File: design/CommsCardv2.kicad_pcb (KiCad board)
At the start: 4 copper layers, 204 parts, among them J1001 USB_B, J201 Conn_01x02, J301 DB9_Male_MountingHoles, J302 DB9_Male_MountingHoles, J303 DB9_Male_MountingHoles, J304 Conn_01x02, J305 Conn_Coaxial, J501 Conn_01x03, J701 Conn_01x03, J901 USB_B, Q301 Q_NMOS_DGS, Q302 Q_NMOS_DGS, U1001 ADUM3160, U201 LT3509EMSE, U301 MAX3387EEUG, U302 MAX3485, U303 TPS28225DRBT, U401 STWD100xxWY, U402 STWD100xxWY, U403 74LVC2G00, U405 74AHC157, U406 74LV14, U501 93C46B, U502 FT4232H, U503 74LV595, U601 SN74LV86, U602 74LVC3G14, U603 74LVC1G80, U604 74LVC2G86, U605 74LV595, U606 74LV595, U607 74LVC2G86, U701 93C46B, U702 FT4232H, U703 74LV595, U801 SN74LV86, U802 74LVC3G14, U803 74LVC1G80, U804 74LV595, U805 74LVC2G86, U806 74LV595, U807 74LVC2G86, U808 74LVC3G14, U809 74LVC3G14, U810 74LVC3G14, U901 ADUM3160, Y501 ABM8G, Y701 ABM8G

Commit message: Placing caps
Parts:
- removed C502, C505, C702, C705: 27pF, Capacitor_SMD:C_0603_1608Metric
- removed Y501, Y701: ABM8G, Crystal:Crystal_SMD_Abracon_ABM8G-4Pin_3.2x2.5mm
- added C516: 10nF, Capacitor_SMD:C_0603_1608Metric, F.Cu at (158.8, 74.9)
- added C716: 10nF, Capacitor_SMD:C_0603_1608Metric, F.Cu at (187.5, 74.0)
- added R513: 10k, Resistor_SMD:R_0603_1608Metric, F.Cu at (167.0, 71.1)
- added R713: 10k, Resistor_SMD:R_0603_1608Metric, F.Cu at (187.5, 68.6)
- added X501: ASEMB-12MHz, Oscillator:Oscillator_SMD_Abracon_ASE-4Pin_3.2x2.5mm, F.Cu at (158.8, 72.5)
- added X701: ASEMB-12MHz, Oscillator:Oscillator_SMD_Abracon_ASE-4Pin_3.2x2.5mm, F.Cu at (179.5, 69.4)
- L501, L502, L701, L702: footprint Resistor_SMD:R_0603_1608Metric -> Resistor_SMD:R_1210_3225Metric
- moved L502 170.6 mm to (164.5, 66.0), turned to 90 degrees
- moved C508 166.3 mm to (148.0, 71.1), turned to 270 degrees
- moved R509 156.2 mm to (163.8, 79.5)
- moved C513 155.8 mm to (154.9, 71.1), turned to 90 degrees
- moved L501 154.4 mm to (141.0, 66.7), turned to 180 degrees
- moved R510 152.2 mm to (163.8, 76.9)
- moved R507 150.3 mm to (141.6, 79.5), turned to 180 degrees
- moved R508 148.2 mm to (148.6, 85.1), turned to 270 degrees
- moved C507 146.5 mm to (158.8, 82.6)
- moved C512 145.6 mm to (142.2, 74.9), turned to 180 degrees
- moved C514 145.0 mm to (146.7, 85.1), turned to 270 degrees
- moved C506 144.0 mm to (153.0, 71.1), turned to 90 degrees
- moved R511 141.4 mm to (163.8, 75.0)
- moved C501 139.5 mm to (161.9, 66.7), turned to 90 degrees
- moved C510 134.5 mm to (158.8, 77.5)
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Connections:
- net Net-(R501-Pad2) renamed /FlightComputer1/REF
- net Net-(R701-Pad2) renamed /FlightComputer2/REF
- C503 pad 1: Net-(C501-Pad1) -> Net-(C503-Pad1)
- C508 pad 1: Net-(C501-Pad1) -> Net-(C503-Pad1)
- C703 pad 1: Net-(C701-Pad1) -> Net-(C703-Pad1)
- C708 pad 1: Net-(C701-Pad1) -> Net-(C703-Pad1)
- L501 pad 1: Net-(C501-Pad1) -> Net-(C503-Pad1)
- L502 pad 1: GND -> Net-(C501-Pad1)
- L701 pad 1: Net-(C701-Pad1) -> Net-(C703-Pad1)
- L702 pad 1: GND -> Net-(C701-Pad1)
- U502 pad 3: Net-(C502-Pad1) -> /FlightComputer1/OSCI
- U502 pad 5: GND -> Net-(C501-Pad1)
- U502 pad 9: Net-(C501-Pad1) -> Net-(C503-Pad1)
- U702 pad 3: Net-(C702-Pad1) -> /FlightComputer2/OSCI
- U702 pad 5: GND -> Net-(C701-Pad1)
- U702 pad 9: Net-(C701-Pad1) -> Net-(C703-Pad1)
- U810 pad 3: Net-(U810-Pad3) -> (no net)
- U810 pad 4: (no net) -> GND
- U810 pad 5: Net-(U810-Pad5) -> (no net)
- U810 pad 8: (no net) -> +3V3

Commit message: Annotating
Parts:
- removed the C509 at (103.4, 219.3)
- removed C515, C608, C609, C715, C808, C809: 0u1F, Capacitor_SMD:C_0603_1608Metric
- removed the C601 at (89.5, 253.4)
- removed the C709 at (213.0, 159.5)
- removed the C801 at (155.2, 250.9)
- removed the U607 at (100.8, 248.3)
- removed the U802 at (144.4, 246.7)
- removed the U805 at (169.8, 236.6)
- removed U807: 74LVC2G86, Package_SO:MSOP-8_3x3mm_P0.65mm
- removed U808, U809, U810: 74LVC3G14, Package_SO:VSSOP-8_2.3x2mm_P0.5mm
- added C602: 0u1F, Capacitor_SMD:C_0603_1608Metric, F.Cu at (54.0, 156.9)
- added C802: 0u1F, Capacitor_SMD:C_0603_1608Metric, F.Cu at (69.8, 156.9)
- added U801: 74LVC3G14, Package_SO:VSSOP-8_2.3x2mm_P0.5mm, F.Cu at (161.9, 246.4)
- added U803: 501BMILF, Package_SO:SOIC-8_3.9x4.9mm_P1.27mm, F.Cu at (63.6, 158.8)
- U603: value 74LVC1G80 -> 501BMILF; footprint Package_TO_SOT_SMD:SOT-353_SC-70-5 -> Package_SO:SOIC-8_3.9x4.9mm_P1.27mm
- U604: value 74LVC2G86 -> 74LVC1G80; footprint Package_SO:MSOP-8_3x3mm_P0.65mm -> Package_TO_SOT_SMD:SOT-353_SC-70-5
- moved C606 188.7 mm to (132.1, 68.6)
- moved U601 186.2 mm to (128.3, 68.6)
- moved D502 182.3 mm to (172.7, 41.3)
- moved U603 175.3 mm to (125.1, 75.6)
- moved D503 174.3 mm to (165.1, 41.3)
- moved U602 169.8 mm to (133.3, 75.6), turned to 180 degrees
- moved U604 159.2 mm to (128.9, 81.3)
- moved C603 155.7 mm to (116.2, 82.5)
- moved U605 150.4 mm to (122.6, 91.4)
- moved U607 146.0 mm to (123.2, 99.7)
- moved J501 135.8 mm to (134.0, 82.5)
- moved X701 92.7 mm to (88.7, 87.9)
- moved C702 92.7 mm to (96.7, 92.4)
- moved R701 92.7 mm to (96.7, 87.1)
- moved D501 5.86 mm to (180.3, 41.3)
- renumbered C405 to C401, C401 to C402, C402 to C403, C403 to C404, C404 to C405, C503 to C501, C516 to C502, C501 to C503, C508 to C504, C506 to C505, C504 to C506, C510 to C508, C511 to C509, C512 to C510, C513 to C511, C514 to C512, C605 to C601, C606 to C605, C602 to C606, C703 to C701, C716 to C702, C701 to C703, C708 to C704, C706 to C705, C704 to C706, C710 to C708, C711 to C709, C712 to C710, C713 to C711, C714 to C712, C803 to C801, C805 to C803, C807 to C805, C802 to C807, R404 to R403, R405 to R404, R406 to R405, R407 to R406, R403 to R407, R513 to R501, R501 to R502, R502 to R503, R503 to R504, R504 to R505, R505 to R506, R506 to R507, R507 to R508, R508 to R509, R509 to R510, R510 to R511, R511 to R512, R512 to R513, R713 to R701, R701 to R702, R702 to R703, R703 to R704, R704 to R705, R705 to R706, R706 to R707, R707 to R708, R708 to R709, R709 to R710, R710 to R711, R711 to R712, R712 to R713, U406 to U401, U403 to U402, U401 to U403, U402 to U404, U602 to U601, U601 to U602, U606 to U607, U801 to U802, U803 to U804, U804 to U805
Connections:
- U601 pad 3: Net-(C601-Pad1) -> (no net)
- U601 pad 5: Net-(C601-Pad2) -> (no net)
- U602 pad 10: /FlightComputer1/LOSComms/DELAY_CLK -> Net-(U602-Pad10)
- U602 pad 3: Net-(U601-Pad3) -> Net-(U602-Pad3)
- U602 pad 4: /FlightComputer1/LOSComms/DELAY_CLK -> /FlightComputer1/LOSComms/DATA
- U602 pad 5: GND -> Net-(U602-Pad5)
- U602 pad 6: Net-(C601-Pad1) -> /FlightComputer1/LOSComms/RNRZ-L
- U602 pad 8: Net-(U601-Pad8) -> Net-(U602-Pad5)
- U602 pad 9: Net-(C601-Pad2) -> Net-(U602-Pad9)
- U603 pad 1: Net-(U601-Pad3) -> /FlightComputer1/LOSComms/DELAY_CLK
- U603 pad 2: Net-(U601-Pad8) -> +3V3
- U603 pad 4: /FlightComputer1/LOSComms/BIPHASE -> Net-(U603-Pad4)
- U603 pad 5: +3V3 -> Net-(U603-Pad5)
- U604 pad 1: /FlightComputer1/LOSComms/DATA -> Net-(U602-Pad3)
- U604 pad 2: Net-(U604-Pad2) -> Net-(U603-Pad5)
- U604 pad 3: Net-(U604-Pad2) -> GND
- U604 pad 4: GND -> /FlightComputer1/LOSComms/BIPHASE
- U604 pad 5: Net-(U604-Pad5) -> +3V3
- U607 pad 4: Net-(U604-Pad5) -> Net-(U602-Pad9)
- U607 pad 5: Net-(U604-Pad6) -> Net-(U602-Pad10)
- U802 pad 10: /FlightComputer2/LOSComms/DELAY_CLK -> Net-(U802-Pad10)
- U802 pad 4: /FlightComputer2/LOSComms/DELAY_CLK -> /FlightComputer2/LOSComms/DATA
- U802 pad 5: GND -> Net-(U802-Pad5)
- U802 pad 6: Net-(C801-Pad1) -> /FlightComputer2/LOSComms/RNRZ-L
- U802 pad 8: Net-(U801-Pad8) -> Net-(U802-Pad5)
- U802 pad 9: Net-(C801-Pad2) -> Net-(U802-Pad9)
- U804 pad 2: Net-(U801-Pad8) -> Net-(U803-Pad5)
- U806 pad 4: Net-(U607-Pad5) -> Net-(U802-Pad9)
- U806 pad 5: Net-(U607-Pad6) (its old number) -> Net-(U802-Pad10)

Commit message: Further Layout work
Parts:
- moved C202 185.2 mm to (122.6, 46.4)
- moved C310 184.0 mm to (330.4, 103.5)
- moved C209 178.6 mm to (111.1, 47.0), turned to 90 degrees
- moved C207 176.9 mm to (120.0, 57.1)
- moved R203 173.3 mm to (118.7, 66.7), turned to 90 degrees
- moved L202 173.1 mm to (118.1, 48.3)
- moved C201 172.1 mm to (122.6, 48.9)
- moved C206 171.8 mm to (125.1, 57.1), turned to 180 degrees
- moved R205 171.7 mm to (117.9, 64.1), turned to 180 degrees
- moved R204 169.9 mm to (127.2, 64.1)
- moved R202 166.4 mm to (126.4, 66.7), turned to 90 degrees
- moved C205 166.0 mm to (120.7, 66.7), turned to 270 degrees
- moved R201 165.2 mm to (122.6, 66.7), turned to 270 degrees
- moved C204 164.4 mm to (124.5, 66.7), turned to 270 degrees
- moved D202 164.2 mm to (116.8, 52.7), turned to 180 degrees
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- renumbered C603 to C601, C601 to C603, C607 to C605, C605 to C606, C606 to C607, U607 to U606
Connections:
- net Net-(C206-Pad1) renamed /Power/BOOST1
- net Net-(C206-Pad2) renamed /Power/SW1
- net Net-(C207-Pad1) renamed /Power/BOOST2
- net Net-(C207-Pad2) renamed /Power/SW2
- net Net-(D201-Pad2) renamed /Power/DA1
- net Net-(D202-Pad2) renamed /Power/DA2
- net Net-(R202-Pad2) renamed /Power/FB1
- net Net-(R203-Pad2) renamed /Power/FB2
- net Net-(U402-Pad6) renamed /Watchdog/FC2_WDO
- U402 pad 1: Net-(U402-Pad1) -> /FlightComputer1/IN_CHARGE
- U402 pad 2: Net-(U402-Pad2) -> /Watchdog/FC1_WDO
- U402 pad 3: Net-(U402-Pad2) -> Net-(R407-Pad1)
- U402 pad 5: /FlightComputer1/IN_CHARGE -> Net-(U402-Pad5)
- U402 pad 7: Net-(R407-Pad1) -> Net-(U402-Pad5)
- U403 pad 1: Net-(U402-Pad1) -> /Watchdog/FC1_WDO
- U601 pad 3: (no net) -> Net-(C807-Pad1)
- U601 pad 5: (no net) -> /FlightComputer2/LOSComms/DELAY_CLK
- U801 pad 3: Net-(C807-Pad1) -> (no net)
- U801 pad 5: /FlightComputer2/LOSComms/DELAY_CLK -> (no net)

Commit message: Further routing
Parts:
- moved R701 125.8 mm to (221.5, 71.1)
- moved X701 125.5 mm to (213.2, 72.5), turned to 180 degrees
- moved C702 117.8 mm to (213.2, 74.9), turned to 180 degrees
- moved L701 112.1 mm to (195.4, 66.7), turned to 180 degrees
- moved R708 106.3 mm to (196.1, 79.5), turned to 180 degrees
- moved C711 100.3 mm to (209.4, 71.1), turned to 90 degrees
- moved C704 97.8 mm to (202.4, 71.1), turned to 270 degrees
- moved R709 95.3 mm to (203.0, 85.1), turned to 270 degrees
- moved C706 94.2 mm to (213.2, 80.7)
- moved C710 92.8 mm to (196.7, 74.9), turned to 180 degrees
- moved C708 92.3 mm to (213.2, 77.5)
- moved C701 91.6 mm to (196.1, 69.8), turned to 180 degrees
- moved C705 88.9 mm to (207.5, 71.1), turned to 90 degrees
- moved C709 87.9 mm to (205.0, 85.1), turned to 270 degrees
- moved J701 85.3 mm to (188.4, 89.5)
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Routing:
- net GND: track 0.00 -> 5.37 mm, vias 0 -> 5
- net /Power/BOOST2: track 0.00 -> 3.78 mm
- net /Power/BOOST1: track 0.00 -> 3.78 mm
- net /Power/SW2: track 0.00 -> 2.62 mm
- net /Power/SW1: track 0.00 -> 2.62 mm
- added copper zone on F.Cu, net /Power/DA1
- added copper zone on F.Cu, net /Power/DA2
- added copper zone on F.Cu, net /Power/PWR_IN
- added copper zone on F.Cu, net /Power/SW2
- added copper zone on In1.Cu, net GND

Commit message: Finish Power layout
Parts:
- moved C501 14.9 mm to (156.5, 69.8)
- moved C502 14.9 mm to (173.6, 74.9)
- moved C505 14.9 mm to (167.9, 71.1)
- moved C506 14.9 mm to (173.6, 80.7)
- moved C507 14.9 mm to (173.6, 82.6)
- moved C508 14.9 mm to (173.6, 77.5)
- moved C509 14.9 mm to (165.4, 85.1)
- moved C511 14.9 mm to (169.8, 71.1)
- moved C512 14.9 mm to (161.5, 85.1)
- moved C901 14.9 mm to (171.7, 46.6)
- moved C903 14.9 mm to (171.7, 62.3)
- moved D501 14.9 mm to (195.2, 41.3)
- moved D502 14.9 mm to (187.6, 41.3)
- moved D503 14.9 mm to (180.0, 41.3)
- moved J901 14.9 mm to (164.5, 41.0)
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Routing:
- net GND: track 5.37 -> 22.4 mm, vias 5 -> 11
- net +3V3: track 0.00 -> 7.26 mm, vias 0 -> 2
- net /Power/FB2: track 0.00 -> 4.32 mm
- net /Power/FB1: track 0.00 -> 4.32 mm
- net Net-(R201-Pad1): track 0.00 -> 2.57 mm
- net Net-(C205-Pad1): track 0.00 -> 2.53 mm
- net Net-(C204-Pad1): track 0.00 -> 2.53 mm
- added copper zone on F.Cu, net +3V3
- added copper zone on F.Cu, net +5V
- added copper zone on F.Cu, net /Power/SW1
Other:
- net class NetConn added: clearance 0.2, trace_width 0.3, via_dia 0.8, via_drill 0.4
- board text added: "+3V3"
- board text added: "+5V"

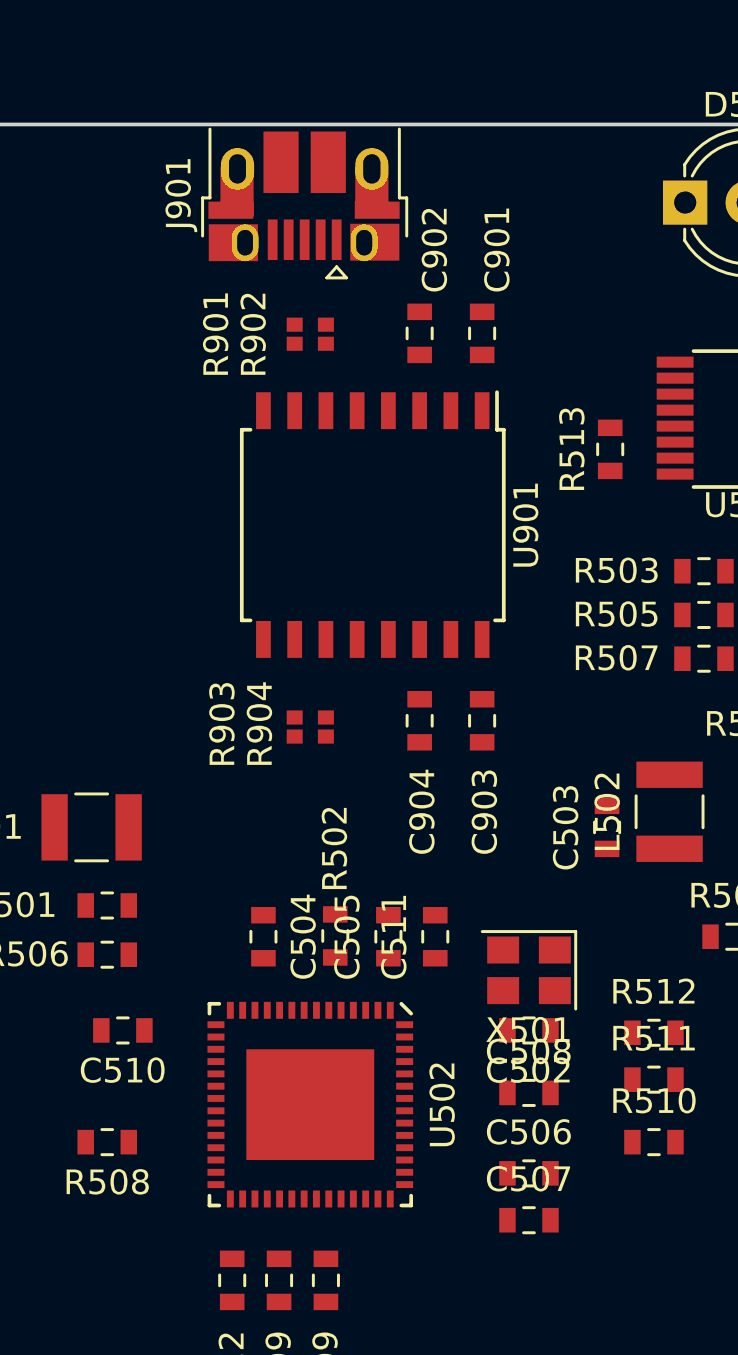
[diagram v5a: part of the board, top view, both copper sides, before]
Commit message: Layout USB Interface
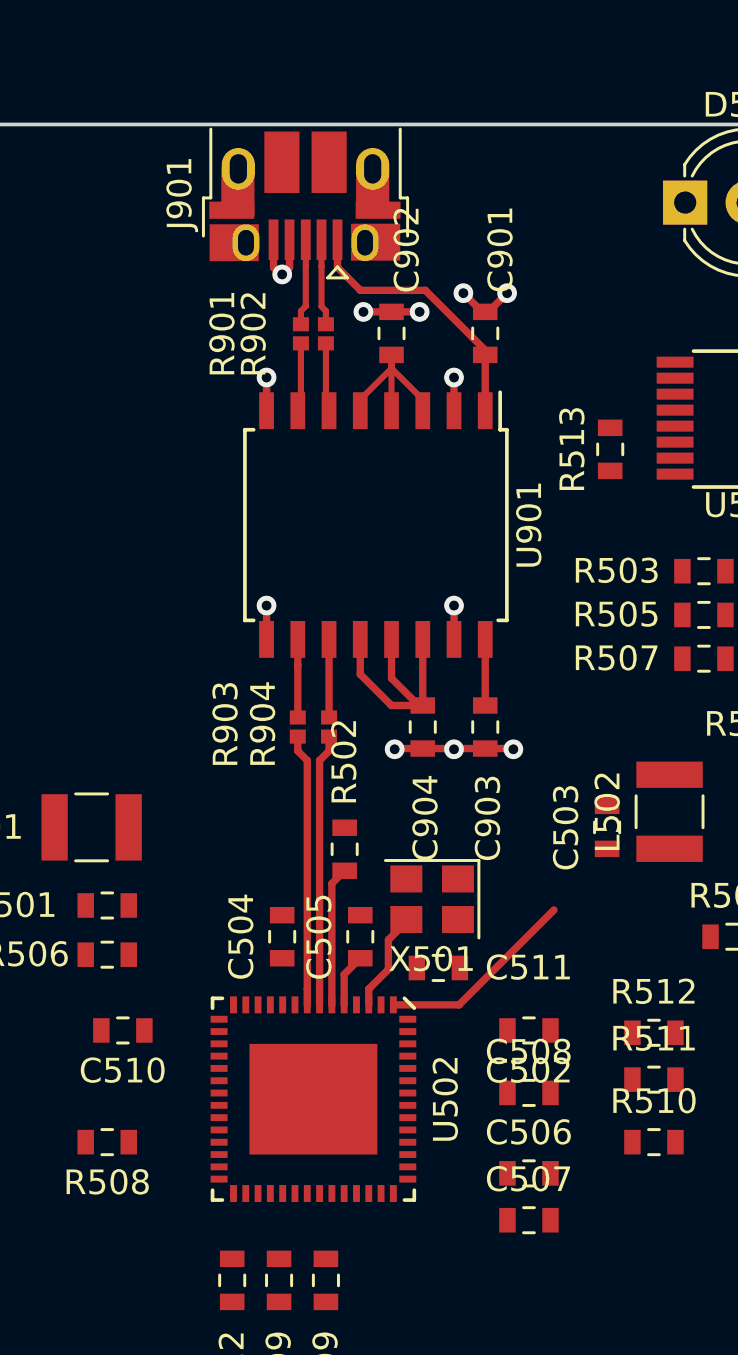
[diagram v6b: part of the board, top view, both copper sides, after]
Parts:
- moved X501 4.88 mm to (169.7, 69.6)
- moved R502 3.54 mm to (166.1, 67.6)
- moved C511 1.28 mm to (169.9, 72.4), turned to 0 degrees
- moved C505 1.14 mm to (166.8, 71.1)
- moved C902 1.14 mm to (168.0, 46.6)
- moved C504 0.76 mm to (163.6, 71.1), turned to 90 degrees
- moved C904 0.28 mm to (169.3, 62.6)
- moved C903 0.28 mm to (171.8, 62.6)
- moved U502 0.26 mm to (164.8, 77.7)
- moved R901 0.25 mm to (164.3, 46.6)
- moved R903 0.13 mm to (164.2, 62.6)
- moved U901 0.13 mm to (167.4, 54.4)
- moved C901 0.13 mm to (171.8, 46.6)
- moved R904 0.13 mm to (165.5, 62.6)
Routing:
- net /FC1_USB/VBUS2: track 0.00 -> 13.2 mm
- net /FC1_USB/USB_DP: track 0.00 -> 11.1 mm
- net /FC1_USB/USB_DM: track 0.00 -> 11.1 mm
- net /FC1_USB/USB_PWR: track 0.00 -> 11.0 mm
- net /FC1_USB/USB_GND: track 0.00 -> 10.5 mm, vias 0 -> 7
- net /FlightComputer1/EECS: track 0.00 -> 8.13 mm
- net GND: track 22.4 -> 30.1 mm, vias 11 -> 16
- net Net-(C902-Pad1): track 0.00 -> 7.31 mm
- net /FlightComputer1/REF: track 0.00 -> 5.67 mm
- net /FlightComputer1/OSCI: track 0.00 -> 4.10 mm
- net Net-(J901-Pad3): track 0.00 -> 3.52 mm
- net Net-(J901-Pad2): track 0.00 -> 3.51 mm
- net Net-(R904-Pad2): track 0.00 -> 3.17 mm
- net Net-(R903-Pad2): track 0.00 -> 3.17 mm
- net Net-(R902-Pad1): track 0.00 -> 2.79 mm
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- added copper zone on GND1.Cu, net /FC1_USB/USB_GND
- added copper zone on GND1.Cu, net GND
- removed copper zone on In1.Cu, net GND
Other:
- net class Default: trace_width 0.25 -> 0.3
- net class ThinNet added: clearance 0.2, trace_width 0.2, via_dia 0.6, via_drill 0.35
